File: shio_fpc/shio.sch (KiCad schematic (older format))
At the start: 86 parts, among them J1 10118193-0001LF, U1 LM66100DCKT, U2 MAX38640AENT+T, U3 NRF52840-CKAA-R7, U4 LM66100DCKT, U5 BMA400, U6 W25N01GVZEIG_TR, U8 SiP32431DR3, Y1 32.768kHz, Y3 32MHz

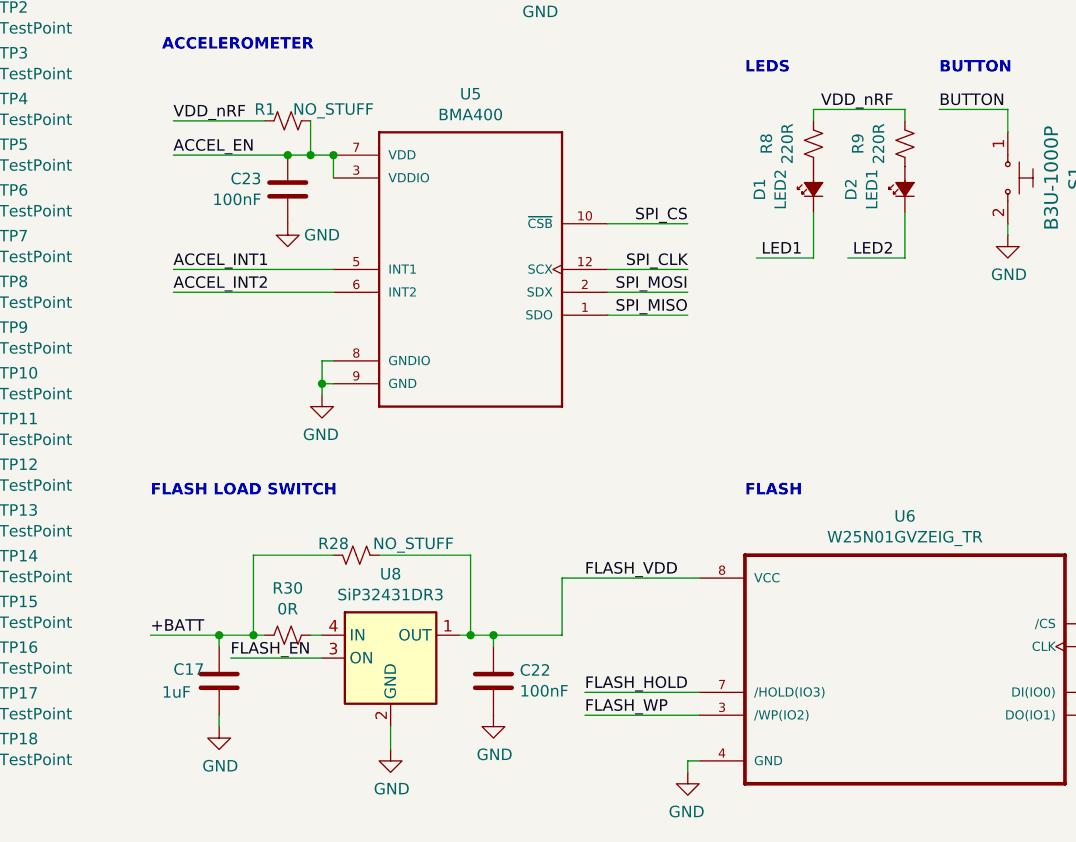
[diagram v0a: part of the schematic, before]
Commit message: Add Udon PCB working docs, Shio BOM, sch changes
Adding Udon PCB subfolder with supporting items
updating the BOM of Shio PCB for 2nd build of Rev A.
Notably, L1 max current increased, D1 changed to red for higher luminosity, LED1 and LED2 value swtiched to correspond to nets
New BOM is exported
Digikey PNs added in sch for most parts
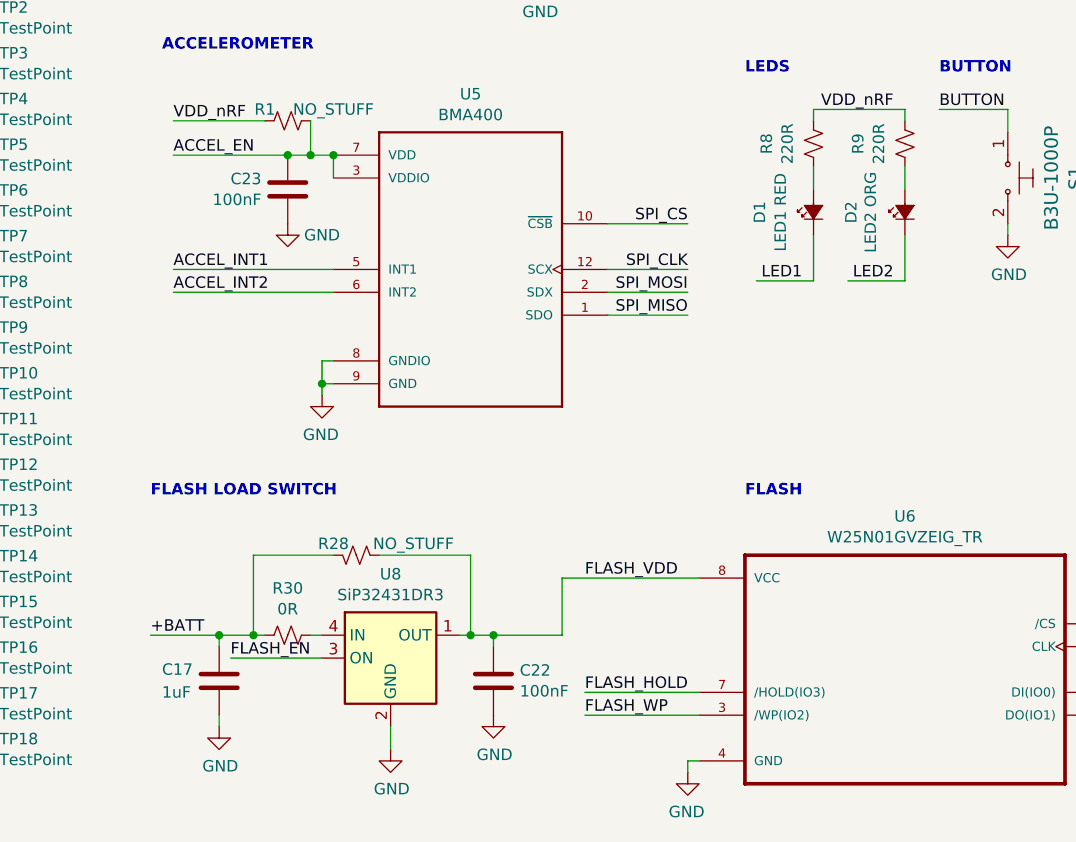
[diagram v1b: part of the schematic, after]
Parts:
- BT1: Digi-Key_PN (none) -> BAT-HLD-001-THM-ND
- C1, C12: Digi-Key_PN (none) -> 490-13339-1-ND; MPN (none) -> GRM155R70J105KA12J; Manufacturer (none) -> Murata Electronics
- C10: Digi-Key_PN (none) -> 490-16368-1-ND; MPN (none) -> GRM0335C1E821JA01D; Manufacturer (none) -> Murata Electronics
- C11, C17, C5: Description Capacitor, 0201, X5R, ±10% -> Capacitor, 0402, X5R, ±10%; Digi-Key_PN (none) -> 1276-1010-1-ND; MPN (none) -> CL05A105KQ5NNNC; Manufacturer (none) -> Samsung Electro-Mechanics
- C13, C14, C15: Digi-Key_PN (none) -> 490-10387-1-ND
- C16: Digi-Key_PN (none) -> 712-1181-1-ND; MPN (none) -> 250R05L1R0BV4T; Manufacturer (none) -> Johanson Technology Inc.
- C18, C19, C20, C21: Digi-Key_PN (none) -> 490-11967-1-ND
- C2: Digi-Key_PN (none) -> 1276-1336-1-ND; MPN (none) -> CL03A473KQ3NNNC; Manufacturer (none) -> Samsung Electro-Mechanics
- C22, C23: Digi-Key_PN (none) -> 490-12686-1-ND
- C24: Digi-Key_PN 500R07S1R0BV4T -> 712-1266-1-ND; MPN (none) -> 500R07S1R0BV4T
- C3, C7: Description Capacitor, 0402, X7R, ±10% -> Capacitor, 0402, X5R, ±10%; Digi-Key_PN (none) -> 1276-1480-1-ND; MPN (none) -> CL05A475KP5NRNC; Manufacturer (none) -> Samsung Electro-Mechanics
- C4: Description Capacitor, 0201, X5R, ±10% -> Capacitor, 0402, X5R, ±10%; Digi-Key_PN (none) -> 1276-7090-1-ND; MPN (none) -> CL05A226MQ5N6J8; Manufacturer (none) -> Samsung Electro-Mechanics
- C6: Description Capacitor, X7R, ±10% -> Capacitor, 0201, X7R, ±10%; Digi-Key_PN (none) -> 1276-1013-1-ND; MPN (none) -> CL03A104KQ3NNNC; Manufacturer (none) -> Samsung Electro-Mechanics
- C8: Digi-Key_PN (none) -> 445-8017-1-ND; MPN (none) -> C1005X6S0G475M050BC; Manufacturer (none) -> TDK Corporation
- C9: Description Capacitor, 0201, X5R, ±10% -> Capacitor, 0402, X5R, ±10%; Digi-Key_PN (none) -> 1276-1450-1-ND; MPN (none) -> CL05A106MP5NUNC; Manufacturer (none) -> Samsung Electro-Mechanics
- D1: value LED2 -> LED1 RED; Digi-Key_PN 350-4450-1-ND -> 350-4447-1-ND
- D2: value LED1 -> LED2 ORG
- L1: Description 250mA Peak Current -> Min 250mA Peak Current; Digi-Key_PN (none) -> 732-7447860022CT-ND; MPN (none) -> 7447860022; Manufacturer (none) -> Würth Elektronik
- L2: Digi-Key_PN (none) -> 490-5570-1-ND
- L3: Digi-Key_PN (none) -> 445-6755-1-ND; Manufacturer TDK -> TDK Corporation
- L4: Digi-Key_PN (none) -> 445-174884-1-ND; MPN (none) -> MLG0603PPA3N9CT000; Manufacturer (none) -> TDK Corporation
- L5: Digi-Key_PN (none) -> 490-7788-1-ND; MPN (none) -> LQP03TN4N7H02D; Manufacturer (none) -> Murata Electronics
- L6: Description (none) -> 3.9nH Unshielded Multilayer Inductor 300mA 220mOhm Max 0402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; Digi-Key_PN L-07C3N9SV6T -> 712-1459-1-ND; MPN (none) -> L-07C3N9SV6T; Manufacturer (none) -> Johanson Technology Inc.
- L7: Description (none) -> 2.7nH Unshielded Multilayer Inductor 300mA 170mOhm Max 0402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; Digi-Key_PN L-07C2N7SV6T -> 712-1415-1-ND; MPN (none) -> L-07C2N7SV6T; Manufacturer (none) -> Johanson Technology Inc.
- MK1: Digi-Key_PN (none) -> 1428-1064-1-ND
- R19, R2, R20, R21, R22, R23, R25, R33, R5: Description (none) -> RES SMD 0 OHM JUMPER 1/20W 0201; Digi-Key_PN (none) -> 311-0.0NCT-ND; MPN (none) -> RC0201JR-070RL; Manufacturer (none) -> Yageo
- R30, R6, R7: Digi-Key_PN (none) -> 311-0.0LRCT-ND; MPN (none) -> RC0402FR-070RL; Manufacturer (none) -> Yageo
- R8, R9: Digi-Key_PN (none) -> 311-220NCT-ND; MPN (none) -> RC0201JR-07220RL; Manufacturer (none) -> Yageo
- U1, U4: Description (none) -> OR Controller P-Channel 1:1 SC-70-6; MPN (none) -> LM66100DCKT; Manufacturer (none) -> Texas Instruments
- U8: Digi-Key_PN (none) -> SIP32431DR3-T1GE3CT-ND
- Y1: Digi-Key_PN (none) -> 644-1155-1-ND
- Y3: Digi-Key_PN (none) -> 1908-1284-1-ND
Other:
- moved on the sheet: D1, D2

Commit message: Pushing new BOM, and BOM config
Can now use KiBOM_CLI.py plugin with BOM.ini file to produce BOMs importable into DigiKey’s BOM manager.
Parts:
- R30: value 0R -> NO_STUFF
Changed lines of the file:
@@
 P 2800 6900
 F 0 "R30" V 2595 6900 50  0000 C CNN
-F 1 "0R" V 2686 6900 50  0000 C CNN
+F 1 "NO_STUFF" V 2686 6900 50  0000 C CNN
 F 2 "Resistor_SMD:R_0402_1005Metric" H 2800 6900 50  0001 C CNN
 F 3 "~" H 2800 6900 50  0001 C CNN

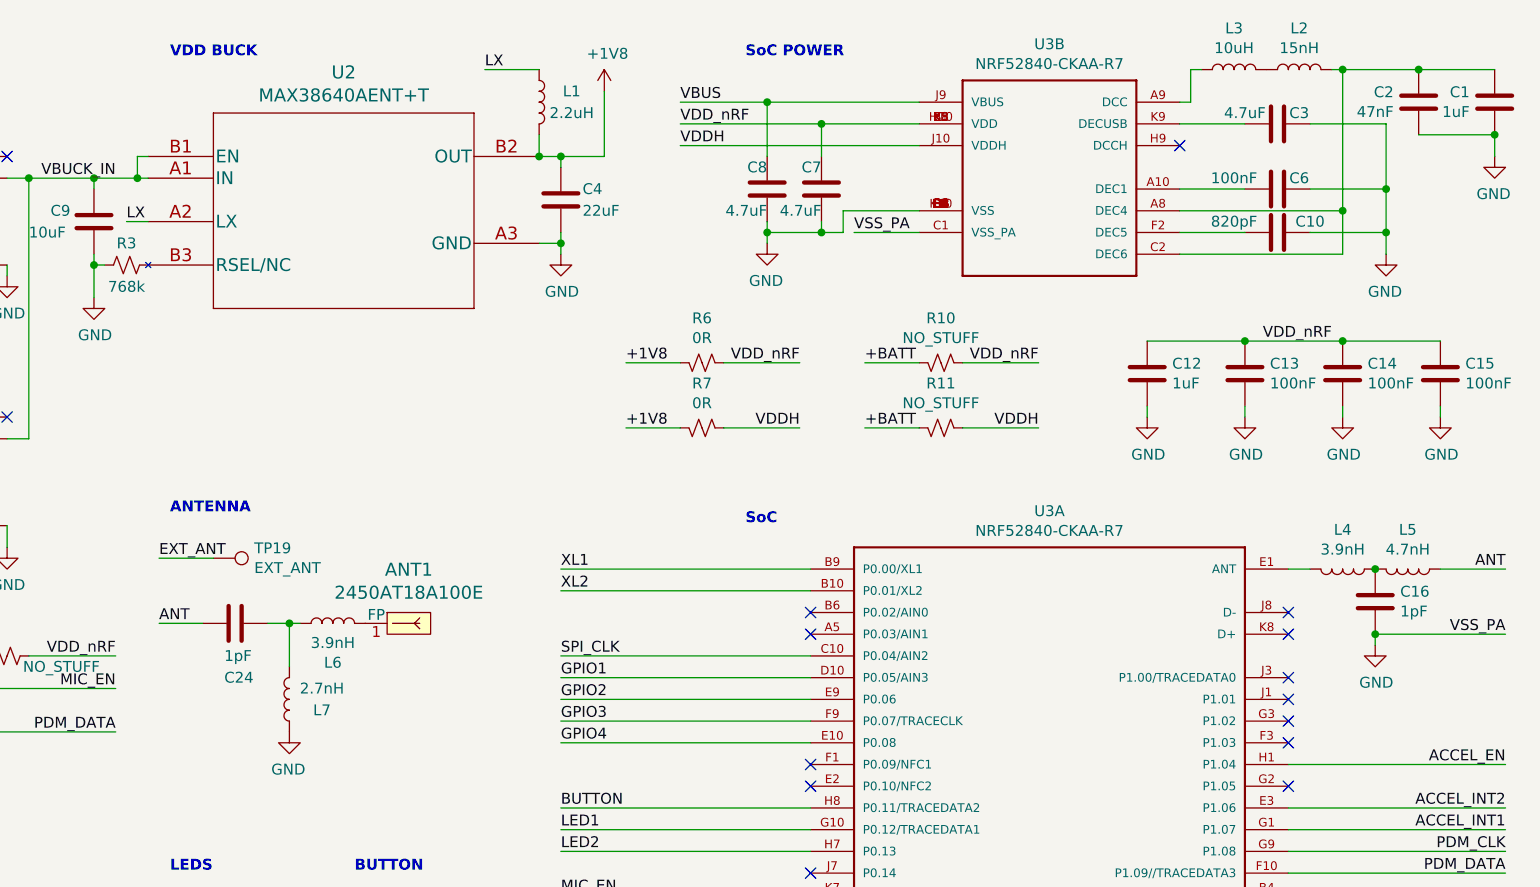
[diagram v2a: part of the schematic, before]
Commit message: Updated antenna components
Antenna path components udpated — new BOM, sch, and PCB generated
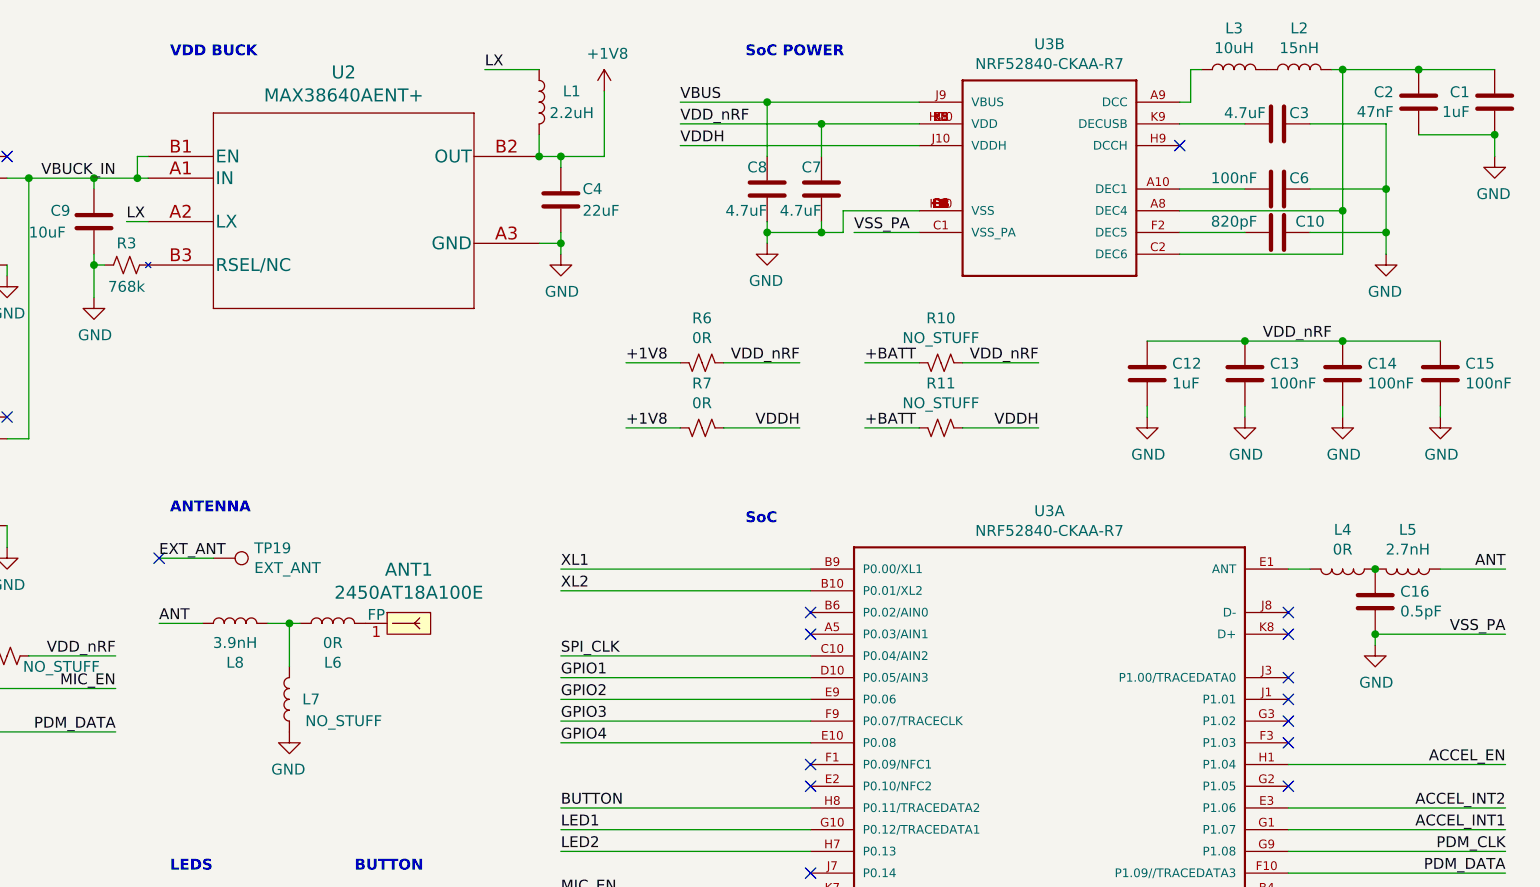
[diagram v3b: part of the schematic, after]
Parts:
- removed C24: 1pF, Capacitor_SMD:C_0201_0603Metric, symbol Device:C
- added L8: 3.9nH, Inductor_SMD:L_0201_0603Metric, symbol Device:L
- C16: value 1pF -> 0.5pF; Digi-Key_PN 712-1181-1-ND -> 712-1467-1-ND; MPN 250R05L1R0BV4T -> 250R05L0R5BV4T
- L4: value 3.9nH -> 0R; Description High frequency chip inductor ±5% -> RES SMD 0 OHM JUMPER 1/20W 0201; Digi-Key_PN 445-174884-1-ND -> 311-0.0NCT-ND; MPN MLG0603PPA3N9CT000 -> RC0201JR-070RL; Manufacturer TDK Corporation -> Yageo
- L5: value 4.7nH -> 2.7nH; Digi-Key_PN 490-7788-1-ND -> 490-16634-1-ND; MPN LQP03TN4N7H02D -> LQP03TN2N7BZ2D
- L6: value 3.9nH -> 0R; Description 3.9nH Unshielded Multilayer Inductor 300mA 220mOhm Max 0402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 -> RES SMD 0 OHM JUMPER 1/20W 0201; Digi-Key_PN 712-1459-1-ND -> 311-0.0NCT-ND; MPN L-07C3N9SV6T -> RC0201JR-070RL; Manufacturer Johanson Technology Inc. -> Yageo
- L7: value 2.7nH -> NO_STUFF
- U2: value MAX38640AENT+T -> MAX38640AENT+; MPN MAX38640AENT+T -> MAX38640AENT+
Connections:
- net ANT: now also L8.1
- net at L6.1, L7.2: now also L8.2
- no-connect marks 26 -> 27
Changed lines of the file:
@@
 Sheet 1 1
 Title "Shio"
-Date "2020-06-08"
-Rev "A"
+Date "2020-12-14"
+Rev "A, Fab: 2"
 Comp "University of Washington"
-Comment1 "Author: Maruchi Kim, Ishan Chatterjee"
+Comment1 "Author: Ishan Chatterjee, Maruchi Kim"
 Comment2 ""
 Comment3 ""
@@
 P 4700 1150
 F 0 "U2" H 5600 1537 60  0000 C CNN
-F 1 "MAX38640AENT+T" H 5600 1431 60  0000 C CNN
+F 1 "MAX38640AENT+" H 5600 1431 60  0000 C CNN
 F 2 "Shio:MAX38640AENT&plus_" H 5600 1390 60  0001 C CNN
 F 3 "https://www.mouser.com/datasheet/2/256/MAX38640A-MAX38643B-1622807.pdf" H 4700 1150 60  0001 C CNN
-F 4 "MAX38640AENT+T" H 4700 1150 50  0001 C CNN "MPN"
+F 4 "MAX38640AENT+" H 4700 1150 50  0001 C CNN "MPN"
 	1    4700 1150
 	1    0    0    -1
@@
 Text Label 10950 3050 2    50   ~ 0
 ANT
-$Comp
-L Device:C C24
-U 1 1 5EEC9FE3
-P 5100 3300
-F 0 "C24" V 5350 3250 50  0000 L CNN
-F 1 "1pF" V 5250 3250 50  0000 L CNN
-F 2 "Capacitor_SMD:C_0201_0603Metric" H 5138 3150 50  0001 C CNN
-F 3 "~" H 5100 3300 50  0001 C CNN
-F 4 "712-1266-1-ND" V 5100 3300 50  0001 C CNN "Digi-Key_PN"
-F 5 "500R07S1R0BV4T" H 5100 3300 50  0001 C CNN "MPN"
-	1    5100 3300
-	0    1    1    0
-$EndComp
 Text Label 4750 3300 0    50   ~ 0
 ANT
@@
 Wire Wire Line
 	4550 5500 4200 5500
-$Comp
-L Device:L L6
-U 1 1 5EECA836
-P 5550 3300
-F 0 "L6" V 5369 3300 50  0000 C CNN
-F 1 "3.9nH" V 5460 3300 50  0000 C CNN
-F 2 "Inductor_SMD:L_0201_0603Metric" H 5550 3300 50  0001 C CNN
-F 3 "~" H 5550 3300 50  0001 C CNN
-F 4 "712-1459-1-ND" V 5550 3300 50  0001 C CNN "Digi-Key_PN"
-F 5 "3.9nH Unshielded Multilayer Inductor 300mA 220mOhm Max 0402 (1005 Metric) " H 5550 3300 50  0001 C CNN "Description"
-F 6 "L-07C3N9SV6T" H 5550 3300 50  0001 C CNN "MPN"
-F 7 "Johanson Technology Inc." H 5550 3300 50  0001 C CNN "Manufacturer"
-	1    5550 3300
-	0    -1   -1   0
-$EndComp
 $Comp
 L dk_RF-Antennas:2450AT18A100E ANT1
@@
 U 1 1 5EECA3DD
 P 5350 3650
-F 0 "L7" H 5200 3700 50  0000 C CNN
-F 1 "2.7nH" H 5200 3600 50  0000 C CNN
+F 0 "L7" H 5250 3650 50  0000 C CNN
+F 1 "NO_STUFF" H 5100 3750 50  0000 C CNN
 F 2 "Inductor_SMD:L_0201_0603Metric" H 5350 3650 50  0001 C CNN
 F 3 "~" H 5350 3650 50  0001 C CNN
@@
 P 10200 3050
 F 0 "L4" V 10019 3050 50  0000 C CNN
-F 1 "3.9nH" V 10110 3050 50  0000 C CNN
+F 1 "0R" V 10110 3050 50  0000 C CNN
 F 2 "Inductor_SMD:L_0201_0603Metric" H 10200 3050 50  0001 C CNN
 F 3 "~" H 10200 3050 50  0001 C CNN
-F 4 "High frequency chip inductor ±5%" V 10200 3050 50  0001 C CNN "Description"
-F 5 "445-174884-1-ND" H 10200 3050 50  0001 C CNN "Digi-Key_PN"
-F 6 "MLG0603PPA3N9CT000" H 10200 3050 50  0001 C CNN "MPN"
-F 7 "TDK Corporation" H 10200 3050 50  0001 C CNN "Manufacturer"
+F 4 "RES SMD 0 OHM JUMPER 1/20W 0201" V 10200 3050 50  0001 C CNN "Description"
+F 5 "311-0.0NCT-ND" H 10200 3050 50  0001 C CNN "Digi-Key_PN"
+F 6 "RC0201JR-070RL" H 10200 3050 50  0001 C CNN "MPN"
+F 7 "Yageo" H 10200 3050 50  0001 C CNN "Manufacturer"
 	1    10200 3050
 	0    1    1    0
@@
 P 10500 3050
 F 0 "L5" V 10319 3050 50  0000 C CNN
-F 1 "4.7nH" V 10410 3050 50  0000 C CNN
+F 1 "2.7nH" V 10410 3050 50  0000 C CNN
 F 2 "Inductor_SMD:L_0201_0603Metric" H 10500 3050 50  0001 C CNN
 F 3 "~" H 10500 3050 50  0001 C CNN
 F 4 "High frequency chip inductor ±5%" V 10500 3050 50  0001 C CNN "Description"
-F 5 "490-7788-1-ND" H 10500 3050 50  0001 C CNN "Digi-Key_PN"
-F 6 "LQP03TN4N7H02D" H 10500 3050 50  0001 C CNN "MPN"
+F 5 "490-16634-1-ND" H 10500 3050 50  0001 C CNN "Digi-Key_PN"
+F 6 "LQP03TN2N7BZ2D" H 10500 3050 50  0001 C CNN "MPN"
 F 7 "Murata Electronics" H 10500 3050 50  0001 C CNN "Manufacturer"
 	1    10500 3050
@@
 P 10350 3200
 F 0 "C16" H 10465 3246 50  0000 L CNN
-F 1 "1pF" H 10465 3155 50  0000 L CNN
+F 1 "0.5pF" H 10465 3155 50  0000 L CNN
 F 2 "Capacitor_SMD:C_0201_0603Metric" H 10388 3050 50  0001 C CNN
 F 3 "~" H 10350 3200 50  0001 C CNN
 F 4 "Capacitor, 0201, NP0, ±5%" H 10350 3200 50  0001 C CNN "Description"
-F 5 "712-1181-1-ND" H 10350 3200 50  0001 C CNN "Digi-Key_PN"
-F 6 "250R05L1R0BV4T" H 10350 3200 50  0001 C CNN "MPN"
+F 5 "712-1467-1-ND" H 10350 3200 50  0001 C CNN "Digi-Key_PN"
+F 6 "250R05L0R5BV4T" H 10350 3200 50  0001 C CNN "MPN"
 F 7 "Johanson Technology Inc." H 10350 3200 50  0001 C CNN "Manufacturer"
 	1    10350 3200
@@
 Wire Wire Line
 	5100 4950 5100 4850
+$Comp
+L Device:L L8
+U 1 1 5FDAC9F8
+P 5100 3300
+F 0 "L8" V 4919 3300 50  0000 C CNN
+F 1 "3.9nH" V 5010 3300 50  0000 C CNN
+F 2 "Inductor_SMD:L_0201_0603Metric" H 5100 3300 50  0001 C CNN
+F 3 "~" H 5100 3300 50  0001 C CNN
+F 4 "712-1459-1-ND" V 5100 3300 50  0001 C CNN "Digi-Key_PN"
+F 5 "3.9nH Unshielded Multilayer Inductor 300mA 220mOhm Max 0402 (1005 Metric) " H 5100 3300 50  0001 C CNN "Description"
+F 6 "L-07C3N9SV6T" H 5100 3300 50  0001 C CNN "MPN"
+F 7 "Johanson Technology Inc." H 5100 3300 50  0001 C CNN "Manufacturer"
+	1    5100 3300
+	0    -1   -1   0
+$EndComp
+$Comp
+L Device:L L6
+U 1 1 5FDB0BFB
+P 5550 3300
+F 0 "L6" V 5369 3300 50  0000 C CNN
+F 1 "0R" V 5460 3300 50  0000 C CNN
+F 2 "Inductor_SMD:L_0201_0603Metric" H 5550 3300 50  0001 C CNN
+F 3 "~" H 5550 3300 50  0001 C CNN
+F 4 "RES SMD 0 OHM JUMPER 1/20W 0201" V 5550 3300 50  0001 C CNN "Description"
+F 5 "311-0.0NCT-ND" H 5550 3300 50  0001 C CNN "Digi-Key_PN"
+F 6 "RC0201JR-070RL" H 5550 3300 50  0001 C CNN "MPN"
+F 7 "Yageo" H 5550 3300 50  0001 C CNN "Manufacturer"
+	1    5550 3300
+	0    -1   -1   0
+$EndComp
+NoConn ~ 4750 3000
 $EndSCHEMATC
